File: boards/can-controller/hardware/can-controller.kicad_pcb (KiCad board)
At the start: 2 copper layers, 100 x 100 mm, 186 parts, among them J1 RPi_GPIO, J10 CAN1, J11 CAN2, J12 CAN3, J13 CAN4, J2 ICSP, J20 12V IN, J3 UART, J30 RELAY, J4 USB-C, J40 GPIO, J50 ANALOG, Q1 SUD50P04-08, U1 PIC32MK1024MCM064-I/PT, U10 ISO1044BD, U11 ISO1044BD, U12 ISO1044BD, U13 ISO1044BD, U2 MCP1826S-3302E/DB, U20 R-78E5.0-0.5, U21 TLP293, U3 USBLC6-2SC6, U30 ISO6740, U31 ISO6740, U32 ULN2803A, U33 MCP23008-E/SO, U50 MCP3428-E/SL, U60 MCP4922-E/SL, U61 LM4040-2.5, U62 LM358B, U63 TPS61040, Y1 12MHz

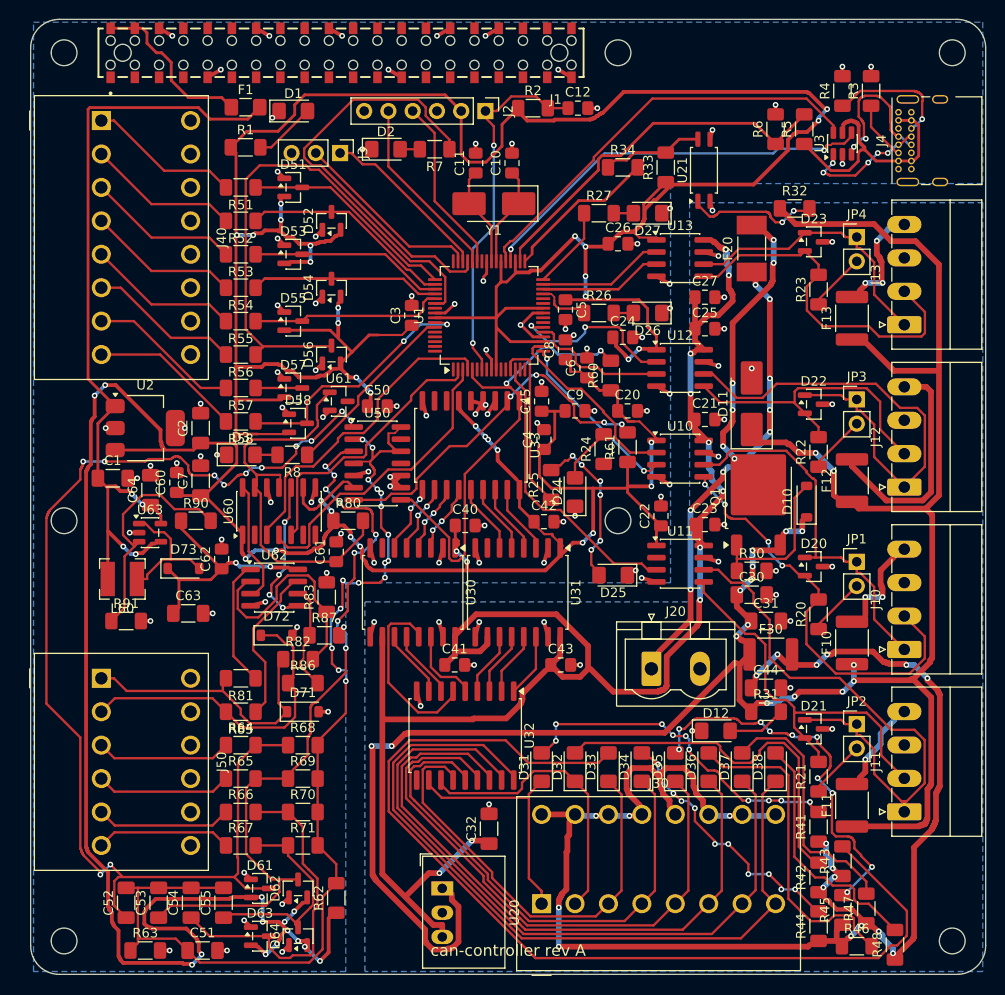
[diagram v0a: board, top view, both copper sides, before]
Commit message: can-controller: rev 6 snapshot (placement, domain pours, ground fanout); POC plan
- PCB reset to 100 x 100 mm with M4 standoff holes, synced from the new
  schematic, first-pass placement (place_rev6.py), domain pours and 2 mm
  isolation keep-outs (zones_rev6.py), 117 ground fanout vias (route_rev6.py).
  Not routed: 100 x 100 mm on 2 layers proved unroutable (Freerouting
  plateaued at ~40 unrouted).
- Net classes: Default 0.2 mm, Power 0.5 mm, PowerQFP 0.25 mm.
- Relay flyback diodes 1N4148W (SOD-123).
- tools/miniroute.py: island joining at cut ends, skips unreachable islands.
- Requirements 4.0: subsystem proof-of-concept boards (<= 100 x 100 mm) and a
  pluggable PIC + power module first; final board <= 115 x 170 mm.

Co-Authored-By: Claude Opus 5.5 <noreply@anthropic.com>
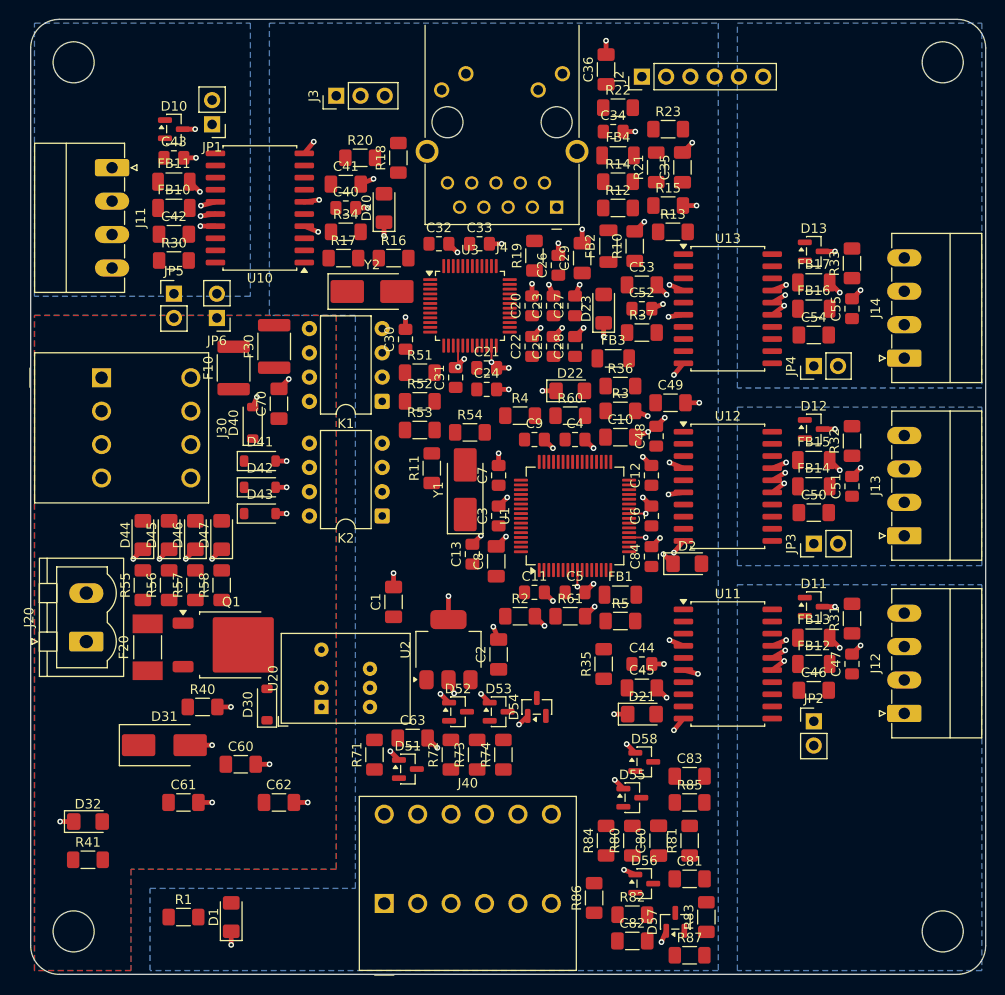
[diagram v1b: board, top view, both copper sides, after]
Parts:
- removed C64: 10uF 25V X7R, Capacitor_SMD:C_1206_3216Metric_Pad1.33x1.80mm_HandSolder
- removed D24, D25, D26, D27: LED yellow, LED_SMD:LED_1206_3216Metric_Pad1.42x1.75mm_HandSolder
- removed D3: LED green, LED_SMD:LED_1206_3216Metric_Pad1.42x1.75mm_HandSolder
- removed D33, D34, D35, D36, D37, D38: LED red, LED_SMD:LED_1206_3216Metric_Pad1.42x1.75mm_HandSolder
- removed D61, D62, D63, D64: BAT54S, Package_TO_SOT_SMD:SOT-23
- removed D71, D72: 15V, Diode_SMD:D_SOD-123
- removed D73: MBR0530, Diode_SMD:D_SOD-123
- removed F1: 0.75A, Fuse:Fuse_1206_3216Metric_Pad1.42x1.75mm_HandSolder
- removed F11, F12, F13: 1.1A, Fuse:Fuse_1812_4532Metric_Pad1.30x3.40mm_HandSolder
- removed J1: RPi_GPIO, Thl_Connector:Samtec_REF-182665_2x20_P2.54mm_PassThrough
- removed J10: CAN1, Connector_Phoenix_MC:PhoenixContact_MC_1,5_4-G-3.5_1x04_P3.50mm_Horizontal
- removed J50: ANALOG, Thl_Connector:PhoenixContact_SPTD_1,5_6-H-3,5_2x06_P3.5mm_Horizontal
- removed L60: 10uH, Inductor_SMD:L_Bourns-SRN4018
- removed MH5, MH6, MH7: MountingHole_2.7mm_M2.5, MountingHole:MountingHole_2.7mm_M2.5
- removed R24, R25, R26, R27, R7, R8: 1k, Resistor_SMD:R_1206_3216Metric_Pad1.30x1.75mm_HandSolder
- removed R42, R43, R44, R45, R46, R47, R48: 4.7k, Resistor_SMD:R_1206_3216Metric_Pad1.30x1.75mm_HandSolder
- removed R6: 100k, Resistor_SMD:R_1206_3216Metric_Pad1.30x1.75mm_HandSolder
- removed R62, R63: 10k, Resistor_SMD:R_1206_3216Metric_Pad1.30x1.75mm_HandSolder
- removed R64, R65, R66, R67: 10M, Resistor_SMD:R_1206_3216Metric_Pad1.30x1.75mm_HandSolder
- removed R68, R69, R70: 130k, Resistor_SMD:R_1206_3216Metric_Pad1.30x1.75mm_HandSolder
- removed R90: 1M, Resistor_SMD:R_1206_3216Metric_Pad1.30x1.75mm_HandSolder
- removed R91: 105k, Resistor_SMD:R_1206_3216Metric_Pad1.30x1.75mm_HandSolder
- removed U21: TLP293, Package_SO:SOIC-4_4.55x2.6mm_P1.27mm
- removed U30, U31: ISO6740, Package_SO:SOIC-16W_7.5x10.3mm_P1.27mm
- removed U32: ULN2803A, Package_SO:SOIC-18W_7.5x11.6mm_P1.27mm
- removed U33: MCP23008-E/SO, Package_SO:SOIC-18W_7.5x11.6mm_P1.27mm
- removed U50: MCP3428-E/SL, Package_SO:SOIC-14_3.9x8.7mm_P1.27mm
- removed U60: MCP4922-E/SL, Package_SO:SOIC-14_3.9x8.7mm_P1.27mm
- removed U61: LM4040-2.5, Package_TO_SOT_SMD:SOT-23
- removed U62: LM358B, Package_SO:SOIC-8_3.9x4.9mm_P1.27mm
- removed U63: TPS61040, Package_TO_SOT_SMD:SOT-23-5
- added C13: 100nF 50V X7R, Capacitor_SMD:C_0805_2012Metric_Pad1.18x1.45mm_HandSolder, F.Cu at (146.2, 156.0)
- added C28: 100nF 50V X7R, Capacitor_SMD:C_0805_2012Metric_Pad1.18x1.45mm_HandSolder, F.Cu at (157.0, 134.2)
- added C29: 3.3uF 25V X7R, Capacitor_SMD:C_1206_3216Metric_Pad1.33x1.80mm_HandSolder, F.Cu at (157.8, 125.0)
- added C33: 100nF 50V X7R, Capacitor_SMD:C_0805_2012Metric_Pad1.18x1.45mm_HandSolder, F.Cu at (147.0, 123.5)
- added C34: 100nF 50V X7R, Capacitor_SMD:C_0805_2012Metric_Pad1.18x1.45mm_HandSolder, F.Cu at (161.0, 111.8)
- added C35: 1uF 50V X7R, Capacitor_SMD:C_1206_3216Metric_Pad1.33x1.80mm_HandSolder, F.Cu at (168.2, 115.5)
- added C36: 1nF 2kV X7R, Capacitor_SMD:C_1206_3216Metric_Pad1.33x1.80mm_HandSolder, F.Cu at (160.2, 105.2)
- added C46: 10uF 25V X7R, Capacitor_SMD:C_1206_3216Metric_Pad1.33x1.80mm_HandSolder, F.Cu at (182.0, 170.2)
- added C47: 100nF 50V X7R, Capacitor_SMD:C_0805_2012Metric_Pad1.18x1.45mm_HandSolder, F.Cu at (186.0, 167.5)
- added C48: 100nF 50V X7R, Capacitor_SMD:C_0805_2012Metric_Pad1.18x1.45mm_HandSolder, F.Cu at (165.5, 143.7)
- added C49: 10uF 25V X7R, Capacitor_SMD:C_1206_3216Metric_Pad1.33x1.80mm_HandSolder, F.Cu at (167.0, 140.2)
- added C70: 10uF 25V X7R, Capacitor_SMD:C_1206_3216Metric_Pad1.33x1.80mm_HandSolder, F.Cu at (126.0, 140.2)
- added C80: 100nF 50V X7R, Capacitor_SMD:C_1206_3216Metric_Pad1.33x1.80mm_HandSolder, F.Cu at (165.8, 186.0)
- added C81: 100nF 50V X7R, Capacitor_SMD:C_1206_3216Metric_Pad1.33x1.80mm_HandSolder, F.Cu at (169.0, 190.0)
- added C82: 100nF 50V X7R, Capacitor_SMD:C_1206_3216Metric_Pad1.33x1.80mm_HandSolder, F.Cu at (163.0, 196.5)
- added C83: 100nF 50V X7R, Capacitor_SMD:C_1206_3216Metric_Pad1.33x1.80mm_HandSolder, F.Cu at (169.0, 179.2)
- added C84: 100nF 50V X7R, Capacitor_SMD:C_0805_2012Metric_Pad1.18x1.45mm_HandSolder, F.Cu at (165.0, 156.2)
- added D13: NUP2105L, Package_TO_SOT_SMD:SOT-23, F.Cu at (182.0, 124.3)
- added D30: 15V, Diode_SMD:D_SOD-123, F.Cu at (124.8, 171.8)
- added D40: 1N4148W, Diode_SMD:D_SOD-123, F.Cu at (123.2, 142.2)
- added D41: 1N4148W, Diode_SMD:D_SOD-123, F.Cu at (124.0, 146.2)
- added D42: 1N4148W, Diode_SMD:D_SOD-123, F.Cu at (124.0, 149.0)
- added D43: 1N4148W, Diode_SMD:D_SOD-123, F.Cu at (124.0, 151.8)
- added D44: LED red, LED_SMD:LED_1206_3216Metric_Pad1.42x1.75mm_HandSolder, F.Cu at (111.8, 154.0)
- added D45: LED red, LED_SMD:LED_1206_3216Metric_Pad1.42x1.75mm_HandSolder, F.Cu at (114.5, 154.0)
- added D46: LED red, LED_SMD:LED_1206_3216Metric_Pad1.42x1.75mm_HandSolder, F.Cu at (117.2, 154.0)
- added D47: LED red, LED_SMD:LED_1206_3216Metric_Pad1.42x1.75mm_HandSolder, F.Cu at (120.0, 154.0)
- added FB1: HI1206P121R-10, Inductor_SMD:L_1206_3216Metric_Pad1.22x1.90mm_HandSolder, F.Cu at (161.8, 160.2)
- added FB10: BLM31KN102SN1L, Inductor_SMD:L_1206_3216Metric_Pad1.22x1.90mm_HandSolder, F.Cu at (115.0, 119.8)
- added FB11: BLM31KN102SN1L, Inductor_SMD:L_1206_3216Metric_Pad1.22x1.90mm_HandSolder, F.Cu at (115.0, 117.0)
- added FB12: BLM31KN102SN1L, Inductor_SMD:L_1206_3216Metric_Pad1.22x1.90mm_HandSolder, F.Cu at (182.0, 167.5)
- added FB13: BLM31KN102SN1L, Inductor_SMD:L_1206_3216Metric_Pad1.22x1.90mm_HandSolder, F.Cu at (182.0, 164.8)
- added FB14: BLM31KN102SN1L, Inductor_SMD:L_1206_3216Metric_Pad1.22x1.90mm_HandSolder, F.Cu at (182.0, 148.9)
- added FB15: BLM31KN102SN1L, Inductor_SMD:L_1206_3216Metric_Pad1.22x1.90mm_HandSolder, F.Cu at (182.0, 146.2)
- added FB16: BLM31KN102SN1L, Inductor_SMD:L_1206_3216Metric_Pad1.22x1.90mm_HandSolder, F.Cu at (182.0, 130.3)
- added FB17: BLM31KN102SN1L, Inductor_SMD:L_1206_3216Metric_Pad1.22x1.90mm_HandSolder, F.Cu at (182.0, 127.5)
- added FB2: HI1206P121R-10, Inductor_SMD:L_1206_3216Metric_Pad1.22x1.90mm_HandSolder, F.Cu at (160.5, 123.8)
- added FB3: HI1206P121R-10, Inductor_SMD:L_1206_3216Metric_Pad1.22x1.90mm_HandSolder, F.Cu at (161.0, 135.5)
- added FB4: HI1206P121R-10, Inductor_SMD:L_1206_3216Metric_Pad1.22x1.90mm_HandSolder, F.Cu at (161.5, 114.2)
- added J14: CAN4, Connector_Phoenix_MC:PhoenixContact_MC_1,5_4-G-3.5_1x04_P3.50mm_Horizontal, F.Cu at (191.5, 135.5)
- added JP5: POWERED GND, Connector_PinHeader_2.54mm:PinHeader_1x02_P2.54mm_Vertical, F.Cu at (115.0, 128.7)
- added JP6: POWERED 12V, Connector_PinHeader_2.54mm:PinHeader_1x02_P2.54mm_Vertical, F.Cu at (119.5, 131.3)
- added K1: AQW212, Package_DIP:DIP-8_W7.62mm, F.Cu at (136.8, 140.0)
- added K2: AQW212, Package_DIP:DIP-8_W7.62mm, F.Cu at (136.8, 152.0)
- added R10: 10k, Resistor_SMD:R_1206_3216Metric_Pad1.30x1.75mm_HandSolder, F.Cu at (163.2, 123.8)
- added R11: 10k, Resistor_SMD:R_1206_3216Metric_Pad1.30x1.75mm_HandSolder, F.Cu at (142.0, 147.0)
- added R12: 10k, Resistor_SMD:R_1206_3216Metric_Pad1.30x1.75mm_HandSolder, F.Cu at (161.5, 119.8)
- added R13: 10k, Resistor_SMD:R_1206_3216Metric_Pad1.30x1.75mm_HandSolder, F.Cu at (167.2, 122.2)
- added R14: 12k, Resistor_SMD:R_1206_3216Metric_Pad1.30x1.75mm_HandSolder, F.Cu at (161.5, 117.0)
- added R15: 300R, Resistor_SMD:R_1206_3216Metric_Pad1.30x1.75mm_HandSolder, F.Cu at (166.8, 119.5)
- added R16: 1M, Resistor_SMD:R_1206_3216Metric_Pad1.30x1.75mm_HandSolder, F.Cu at (138.0, 125.0)
- added R17: 49.9R, Resistor_SMD:R_1206_3216Metric_Pad1.30x1.75mm_HandSolder, F.Cu at (132.8, 125.0)
- added R18: 49.9R, Resistor_SMD:R_1206_3216Metric_Pad1.30x1.75mm_HandSolder, F.Cu at (138.5, 114.5)
- added R19: 49.9R, Resistor_SMD:R_1206_3216Metric_Pad1.30x1.75mm_HandSolder, F.Cu at (152.8, 124.8)
- added R35: 1k, Resistor_SMD:R_1206_3216Metric_Pad1.30x1.75mm_HandSolder, F.Cu at (160.0, 167.5)
- added R36: 1k, Resistor_SMD:R_1206_3216Metric_Pad1.30x1.75mm_HandSolder, F.Cu at (161.8, 138.4)
- added R37: 1k, Resistor_SMD:R_1206_3216Metric_Pad1.30x1.75mm_HandSolder, F.Cu at (164.0, 132.8)
- added R40: 10k, Resistor_SMD:R_1206_3216Metric_Pad1.30x1.75mm_HandSolder, F.Cu at (118.0, 172.0)
- added R72: 330R, Resistor_SMD:R_1206_3216Metric_Pad1.30x1.75mm_HandSolder, F.Cu at (144.0, 177.0)
- added R73: 330R, Resistor_SMD:R_1206_3216Metric_Pad1.30x1.75mm_HandSolder, F.Cu at (146.8, 177.0)
- added R74: 330R, Resistor_SMD:R_1206_3216Metric_Pad1.30x1.75mm_HandSolder, F.Cu at (149.5, 177.0)
- added R84: 130k, Resistor_SMD:R_1206_3216Metric_Pad1.30x1.75mm_HandSolder, F.Cu at (160.2, 186.0)
- added Y2: 25MHz, Crystal:Crystal_SMD_5032-2Pin_5.0x3.2mm_HandSoldering, F.Cu at (135.8, 128.5)
- C10: value 27pF 50V C0G -> 1uF 50V X7R; footprint Capacitor_SMD:C_0805_2012Metric_Pad1.18x1.45mm_HandSolder -> Capacitor_SMD:C_1206_3216Metric_Pad1.33x1.80mm_HandSolder
- C12: value 100nF 50V X7R -> 27pF 50V C0G
- C30, C31: value 10uF 25V X7R -> 8pF 50V C0G; footprint Capacitor_SMD:C_1206_3216Metric_Pad1.33x1.80mm_HandSolder -> Capacitor_SMD:C_0805_2012Metric_Pad1.18x1.45mm_HandSolder
- C32, C44, C51, C7: value 10uF 25V X7R -> 100nF 50V X7R; footprint Capacitor_SMD:C_1206_3216Metric_Pad1.33x1.80mm_HandSolder -> Capacitor_SMD:C_0805_2012Metric_Pad1.18x1.45mm_HandSolder
- C41, C42, C45, C50, C60, C61, C62, C8: value 100nF 50V X7R -> 10uF 25V X7R; footprint Capacitor_SMD:C_0805_2012Metric_Pad1.18x1.45mm_HandSolder -> Capacitor_SMD:C_1206_3216Metric_Pad1.33x1.80mm_HandSolder
- C52, C55: footprint Capacitor_SMD:C_1206_3216Metric_Pad1.33x1.80mm_HandSolder -> Capacitor_SMD:C_0805_2012Metric_Pad1.18x1.45mm_HandSolder
- C53, C54: value 100nF 50V X7R -> 10uF 25V X7R
- C63: value 4.7uF 25V X7R -> 10uF 25V X7R
- D10: value 15V -> NUP2105L; footprint Diode_SMD:D_SOD-123 -> Package_TO_SOT_SMD:SOT-23
- D11: value SMBJ15A -> NUP2105L; footprint Diode_SMD:D_SMB_Handsoldering -> Package_TO_SOT_SMD:SOT-23
- D12: value LED green -> NUP2105L; footprint LED_SMD:LED_1206_3216Metric_Pad1.42x1.75mm_HandSolder -> Package_TO_SOT_SMD:SOT-23
- D20, D21, D22, D23: value NUP2105L -> LED yellow; footprint Package_TO_SOT_SMD:SOT-23 -> LED_SMD:LED_1206_3216Metric_Pad1.42x1.75mm_HandSolder
- D31: value LED red -> SMBJ15A; footprint LED_SMD:LED_1206_3216Metric_Pad1.42x1.75mm_HandSolder -> Diode_SMD:D_SMB_Handsoldering
- D32: value LED red -> LED green
- F10: value 1.1A -> 2A
- J11: value CAN2 -> CAN1
- J12: value CAN3 -> CAN2
- J13: value CAN4 -> CAN3
- J30: footprint Thl_Connector:PhoenixContact_SPTD_1,5_8-H-3,5_2x08_P3.5mm_Horizontal -> Thl_Connector:PhoenixContact_SPTD_1,5_4-H-3,5_2x04_P3.5mm_Horizontal
- J4: value USB-C -> JD0-0004NL; footprint Connector_USB:USB_C_Receptacle_GCT_USB4085 -> Thl_Connector:RJ45_Pulse_JD0-0004NL_Horizontal
- J40: value GPIO -> IO; footprint Thl_Connector:PhoenixContact_SPTD_1,5_8-H-3,5_2x08_P3.5mm_Horizontal -> Thl_Connector:PhoenixContact_SPTD_1,5_6-H-3,5_2x06_P3.5mm_Horizontal
- MH1, MH2, MH3, MH4: value MountingHole_2.7mm_M2.5 -> MountingHole_4.3mm_M4_Standoff7mm; footprint MountingHole:MountingHole_2.7mm_M2.5 -> Thl_Mechanical:MountingHole_4.3mm_M4_Standoff7mm
- R20: value 120R -> 49.9R
- R21: value 120R -> 0R
- R22, R23: value 120R -> 330R
- R3, R4: value 5.1k -> 10k
- R30, R32, R33: value 10k -> 120R
- R31: value 4.7k -> 120R
- R51, R52, R53, R54: value 4.7k -> 470R
- R60, R61: value 4.7k -> 10k
- R71: value 130k -> 330R
- R80: value 1k -> 10M
- R81: value 470R -> 10M
- R82: value 30k -> 10M
- R83: value 10k -> 10M
- R85: value 470R -> 130k
- R86: value 30k -> 130k
- R87: value 10k -> 130k
- U10, U11, U12, U13: value ISO1044BD -> ISOW1044; footprint Package_SO:SOIC-8_3.9x4.9mm_P1.27mm -> Package_SO:SOIC-20W_7.5x12.8mm_P1.27mm
- U20: value R-78E5.0-0.5 -> TDN 5-2411WI; footprint Converter_DCDC:Converter_DCDC_RECOM_R-78E-0.5_THT -> Converter_DCDC:Converter_DCDC_TRACO_TDN_5-xxxxWI_THT
- U3: value USBLC6-2SC6 -> W6100-L; footprint Package_TO_SOT_SMD:SOT-23-6 -> Package_QFP:LQFP-48_7x7mm_P0.5mm
- moved J11 106.9 mm to (108.5, 115.5), turned to -90 degrees
- moved C55 90.5 mm to (186.0, 130.3)
- moved C54 88.2 mm to (182.0, 133.1), turned to 0 degrees
- moved J40 87.2 mm to (137.0, 192.6), turned to 0 degrees
- moved D1 84.6 mm to (121.0, 194.0), turned to 90 degrees
- moved C51 83.6 mm to (186.0, 148.9), turned to 90 degrees
- moved C52 82.4 mm to (164.0, 130.3), turned to 0 degrees
- moved C53 82.1 mm to (164.0, 127.8), turned to 0 degrees
- moved JP1 81.6 mm to (119.0, 111.0), turned to 180 degrees
- moved R1 80.9 mm to (116.0, 194.0)
- moved D10 76.9 mm to (115.0, 111.5), turned to 0 degrees
- moved R41 76.6 mm to (106.0, 188.0), turned to 0 degrees
- moved F20 75.8 mm to (112.2, 165.8)
- moved J30 71.8 mm to (107.4, 137.5), turned to -90 degrees
- moved F10 70.9 mm to (121.2, 136.5)
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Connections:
- net /12 V input/V12_F renamed /12 V input, logic supply/V12_F
- net /12 V input/V12_IN renamed /12 V input, logic supply/V12_IN
- net /MCU, USB, power/D1_A renamed /MCU, logic power/D1_A
- net /MCU, USB, power/PGC2 renamed /MCU, logic power/PGC2
- net /MCU, USB, power/PGD2 renamed /MCU, logic power/PGD2
- C10 pad 1: /MCU, USB, power/OSC1 -> /MCU, logic power/AVDD
- C11 pad 1: /MCU, USB, power/OSC2 -> /MCU, logic power/OSC1
- C12 pad 1: /MCU, USB, power/MCLR -> /MCU, logic power/OSC2
- C20 pad 1: +3V3 -> /Ethernet/1V2D
- C21 pad 1: V5_BUS -> /Ethernet/1V2D
- C21 pad 2: GND_BUS -> GND
- C22 pad 1: +3V3 -> /Ethernet/1V2D
- C23 pad 1: V5_BUS -> /Ethernet/1V2D
- C23 pad 2: GND_BUS -> GND
- C24 pad 1: +3V3 -> /Ethernet/1V2A
- C25 pad 1: V5_BUS -> +3V3
- C25 pad 2: GND_BUS -> GND
- C27 pad 1: V5_BUS -> /Ethernet/3V3A
- C27 pad 2: GND_BUS -> GND
- C30 pad 1: +12V -> /Ethernet/XSCI
- C30 pad 2: GND_BUS -> GND
- C31 pad 1: +12V -> /Ethernet/XSCO
- C31 pad 2: GND_BUS -> GND
- C32 pad 1: V5_BUS -> /Ethernet/TXCT
- C32 pad 2: GND_BUS -> GND
- C41 pad 1: V5_BUS -> +5V
- C41 pad 2: GND_BUS -> GND
- C42 pad 1: +3V3 -> /CAN x4/VISO1
- C42 pad 2: GND -> /CAN x4/GND2_1
- C43 pad 1: V5_BUS -> /CAN x4/VCAN1
- C43 pad 2: GND_BUS -> /CAN x4/GND_CAN1
- C44 pad 1: /Relay drive/V12_RLY -> +3V3
- C44 pad 2: GND_BUS -> GND
- C45 pad 1: +3V3 -> +5V
- C50 pad 1: +3V3 -> /CAN x4/VISO3
- C50 pad 2: GND -> /CAN x4/GND2_3
- C51 pad 1: /Analog in/VMID -> /CAN x4/VCAN3
- C51 pad 2: GND -> /CAN x4/GND_CAN3
- C52 pad 1: /Analog in/AIN1 -> +3V3
- C52 pad 2: /Analog in/VMID -> GND
- C53 pad 1: /Analog in/AIN2 -> +5V
- C53 pad 2: /Analog in/VMID -> GND
- C54 pad 1: /Analog in/AIN3 -> /CAN x4/VISO4
- C54 pad 2: /Analog in/VMID -> /CAN x4/GND2_4
- C55 pad 1: /Analog in/AIN4 -> /CAN x4/VCAN4
- C55 pad 2: /Analog in/VMID -> /CAN x4/GND_CAN4
- C60 pad 1: +3V3 -> +12V
- C60 pad 2: GND -> GND_RACK
- C61 pad 1: /Analog out/VREF -> +12V
- C61 pad 2: GND -> GND_RACK
- C62 pad 1: /Analog out/V13 -> +12V
- C62 pad 2: GND -> GND_RACK
- C63 pad 1: /Analog out/V13 -> +5V
- C9 pad 1: +3V3 -> /MCU, logic power/AVDD
- D10 pad 1: +12V -> /CAN x4/CANH1
- D10 pad 2: /12 V input/Q1_G -> /CAN x4/CANL1
- D11 pad 1: +12V -> /CAN x4/CANH2
- D11 pad 2: GND_BUS -> /CAN x4/CANL2
- D12 pad 1: GND_BUS -> /CAN x4/CANH3
- D12 pad 2: /12 V input/D12_A -> /CAN x4/CANL3
- D2 pad 2: /MCU, USB, power/D2_A -> /MCU, logic power/D2_A
- D20 pad 1: /CAN x4/CANH1 -> GND
- D20 pad 2: /CAN x4/CANL1 -> /CAN x4/D20_A
- D21 pad 1: /CAN x4/CANH2 -> GND
- D21 pad 2: /CAN x4/CANL2 -> /CAN x4/D21_A
- D22 pad 1: /CAN x4/CANH3 -> GND
- D22 pad 2: /CAN x4/CANL3 -> /CAN x4/D22_A
- D23 pad 1: /CAN x4/CANH4 -> GND
- D23 pad 2: /CAN x4/CANL4 -> /CAN x4/D23_A
- D31 pad 1: /Relay drive/RLYO1 -> +12V
- D31 pad 2: /Relay drive/D31_A -> GND_RACK
- D32 pad 1: /Relay drive/RLYO2 -> GND_RACK
- D32 pad 2: /Relay drive/D32_A -> /12 V input, logic supply/D32_A
- D55 pad 3: GPIO5 -> AI1P
- D56 pad 3: GPIO6 -> AI1N
- D57 pad 3: GPIO7 -> AI2P
- D58 pad 3: GPIO8 -> AI2N
- F10 pad 2: /CAN x4/V12_CAN1 -> /CAN x4/V12_F10
- J11 pad 1: /CAN x4/CANH2 -> /CAN x4/CANH1
- J11 pad 2: /CAN x4/CANL2 -> /CAN x4/CANL1
- J11 pad 3: GND_BUS -> /CAN x4/GND_CAN1
- J11 pad 4: /CAN x4/V12_CAN2 -> /CAN x4/V12_CAN1
- J12 pad 1: /CAN x4/CANH3 -> /CAN x4/CANH2
- J12 pad 2: /CAN x4/CANL3 -> /CAN x4/CANL2
- J12 pad 3: GND_BUS -> /CAN x4/GND_CAN2
- J12 pad 4: /CAN x4/V12_CAN3 -> unconnected-(J12-Pin_4-Pad4)
- J13 pad 1: /CAN x4/CANH4 -> /CAN x4/CANH3
- J13 pad 2: /CAN x4/CANL4 -> /CAN x4/CANL3
- J13 pad 3: GND_BUS -> /CAN x4/GND_CAN3
- J13 pad 4: /CAN x4/V12_CAN4 -> unconnected-(J13-Pin_4-Pad4)
- J2 pad 1: /MCU, USB, power/MCLR -> /MCU, logic power/MCLR
- J20 pad 2: GND_BUS -> GND_RACK
- J3 pad 1: /MCU, USB, power/U1TX -> /MCU, logic power/U1TX
- J3 pad 2: /MCU, USB, power/U1RX -> /MCU, logic power/U1RX
- J30 pad 1: /Relay drive/RLYO1 -> /Relay drive/RLYOUT1
- J30 pad 2: /Relay drive/RLYO2 -> /Relay drive/RLYOUT2
- J30 pad 3: /Relay drive/RLYO3 -> /Relay drive/RLYOUT3
- J30 pad 4: /Relay drive/RLYO4 -> /Relay drive/RLYOUT4
- J30 pad 5: /Relay drive/RLYO5 -> GND_RACK
- J30 pad 6: /Relay drive/RLYO6 -> GND_RACK
- J30 pad 7: /Relay drive/RLYO7 -> GND_RACK
- J30 pad 8: /Relay drive/RLYO8 -> GND_RACK
- J4 pad SH: GND -> /Ethernet/CHASSIS
- J40 pad 1: /GPIO/GPIO1_EXT -> /GPIO, analog in/GPIO1_EXT
- J40 pad 11: GND -> /GPIO, analog in/AI1N_EXT
- J40 pad 12: GND -> /GPIO, analog in/AI2N_EXT
- J40 pad 2: /GPIO/GPIO2_EXT -> /GPIO, analog in/GPIO2_EXT
- J40 pad 3: /GPIO/GPIO3_EXT -> /GPIO, analog in/GPIO3_EXT
- J40 pad 4: /GPIO/GPIO4_EXT -> /GPIO, analog in/GPIO4_EXT
- J40 pad 5: /GPIO/GPIO5_EXT -> /GPIO, analog in/AI1P_EXT
- J40 pad 6: /GPIO/GPIO6_EXT -> /GPIO, analog in/AI2P_EXT
- J40 pad 7: /GPIO/GPIO7_EXT -> GND
- J40 pad 8: /GPIO/GPIO8_EXT -> GND
- Q1 pad 1: /12 V input/Q1_G -> /12 V input, logic supply/Q1_G
- R2 pad 1: +3V3 -> /MCU, logic power/USB_DP
- R2 pad 2: /MCU, USB, power/MCLR -> GND
- R20 pad 1: /CAN x4/TERM1 -> /Ethernet/RXCT
- R20 pad 2: /CAN x4/CANL1 -> /Ethernet/RXN
- R21 pad 1: /CAN x4/TERM2 -> /Ethernet/3V3A
- R21 pad 2: /CAN x4/CANL2 -> /Ethernet/JCT
- R22 pad 1: /CAN x4/TERM3 -> +3V3
- R22 pad 2: /CAN x4/CANL3 -> /Ethernet/LEDG_A
- R23 pad 1: /CAN x4/TERM4 -> +3V3
- R23 pad 2: /CAN x4/CANL4 -> /Ethernet/LEDY_A
- R3 pad 1: /MCU, USB, power/CC1 -> /MCU, logic power/USB_DN
- R30 pad 1: /12 V input/Q1_G -> /CAN x4/TERM1
- R30 pad 2: GND_BUS -> /CAN x4/CANL1
- R31 pad 1: +12V -> /CAN x4/TERM2
- R31 pad 2: /12 V input/D12_A -> /CAN x4/CANL2
- R32 pad 1: +12V -> /CAN x4/TERM3
- R32 pad 2: /12 V input/OPTO_A -> /CAN x4/CANL3
- R33 pad 1: +3V3 -> /CAN x4/TERM4
- R33 pad 2: /12 V input/V12_OK_C -> /CAN x4/CANL4
- R34 pad 1: /12 V input/V12_OK_C -> LED_CAN1
- R34 pad 2: V12_OK -> /CAN x4/D20_A
- R4 pad 1: /MCU, USB, power/CC2 -> +3V3
- R4 pad 2: GND -> /MCU, logic power/MCLR
- R41 pad 1: /Relay drive/V12_RLY -> +12V
- R41 pad 2: /Relay drive/D31_A -> /12 V input, logic supply/D32_A
- R5 pad 1: /MCU, USB, power/VBUS_C -> /MCU, logic power/LED_HB
- R5 pad 2: /MCU, USB, power/VBUS -> /MCU, logic power/D2_A
- R51 pad 1: GPIO1 -> RLY1
- R51 pad 2: /GPIO/GPIO1_EXT -> /Relay drive/RLED1
- R52 pad 1: GPIO2 -> RLY2
- R52 pad 2: /GPIO/GPIO2_EXT -> /Relay drive/RLED2
- R53 pad 1: GPIO3 -> RLY3
- R53 pad 2: /GPIO/GPIO3_EXT -> /Relay drive/RLED3
- R54 pad 1: GPIO4 -> RLY4
- R54 pad 2: /GPIO/GPIO4_EXT -> /Relay drive/RLED4
- R55 pad 1: GPIO5 -> /Relay drive/RLYOUT1
- R55 pad 2: /GPIO/GPIO5_EXT -> /Relay drive/D44_A
- R56 pad 1: GPIO6 -> /Relay drive/RLYOUT2
- R56 pad 2: /GPIO/GPIO6_EXT -> /Relay drive/D45_A
- R57 pad 1: GPIO7 -> /Relay drive/RLYOUT3
- R57 pad 2: /GPIO/GPIO7_EXT -> /Relay drive/D46_A
- R58 pad 1: GPIO8 -> /Relay drive/RLYOUT4
- R58 pad 2: /GPIO/GPIO8_EXT -> /Relay drive/D47_A
- R60 pad 2: I2C_SCL -> VMID_REF
- R61 pad 1: +3V3 -> VMID_REF
- R61 pad 2: I2C_SDA -> GND
- R71 pad 1: /Analog in/AIN4 -> GPIO1
- R71 pad 2: /Analog in/VMID -> /GPIO, analog in/GPIO1_EXT
- R80 pad 1: +3V3 -> /GPIO, analog in/AI1P_EXT
- R80 pad 2: /Analog out/VREF -> AI1P
- R81 pad 1: /Analog out/OA1 -> /GPIO, analog in/AI1N_EXT
- R81 pad 2: /Analog out/AO1_EXT -> AI1N
- R82 pad 1: /Analog out/AO1_EXT -> /GPIO, analog in/AI2P_EXT
- R82 pad 2: /Analog out/FB1 -> AI2P
- R83 pad 1: /Analog out/FB1 -> /GPIO, analog in/AI2N_EXT
- R83 pad 2: GND -> AI2N
- R85 pad 1: /Analog out/OA2 -> AI1N
- R85 pad 2: /Analog out/AO2_EXT -> VMID
- R86 pad 1: /Analog out/AO2_EXT -> AI2P
- R86 pad 2: /Analog out/FB2 -> VMID
- R87 pad 1: /Analog out/FB2 -> AI2N
- R87 pad 2: GND -> VMID
- U1 pad 11: unconnected-(U1-RA12/AN10/RPA12-Pad11) -> LED_CAN3
- U1 pad 12: unconnected-(U1-RA11/AN9/RPA11-Pad12) -> LED_CAN4
- U1 pad 13: LED_CAN2 -> unconnected-(U1-RA0/OA2OUT/AN0/C2IN4-/C4IN3-/RPA0-Pad13)
- U1 pad 16: LED_CAN1 -> unconnected-(U1-RB1/PGC3/OA1OUT/VREF+/AN3/C1IN4-/C4IN2-/RPB1/CTED1-Pad16)
- U1 pad 19: +3V3 -> /MCU, logic power/AVDD
- U1 pad 2: DAC_SDI -> RLY1
- U1 pad 23: unconnected-(U1-RC2/OA3IN+/AN8/C3IN1+/C3IN3-/RPC2-Pad23) -> AI2N
- U1 pad 24: unconnected-(U1-RC11/AN11/C1IN2--Pad24) -> AI2P
- U1 pad 27: unconnected-(U1-RE12/AN12/C2IN2-/C5IN2-/SDA4-Pad27) -> AI1P
- U1 pad 28: unconnected-(U1-RE13/AN13/C3IN2-/SCL4-Pad28) -> AI1N
- U1 pad 29: LED_CAN3 -> unconnected-(U1-RE14/AN14/RPE14-Pad29)
- U1 pad 3: DAC_SCK -> RLY2
- U1 pad 32: LED_CAN4 -> unconnected-(U1-RB4/RPB4/SCL2-Pad32)
- U1 pad 33: V12_OK -> VMID_REF
- U1 pad 34: /MCU, USB, power/VBUS -> GND
- U1 pad 36: /MCU, USB, power/USB_DN -> /MCU, logic power/USB_DN
- U1 pad 37: /MCU, USB, power/USB_DP -> /MCU, logic power/USB_DP
- U1 pad 39: /MCU, USB, power/OSC1 -> /MCU, logic power/OSC1
- U1 pad 4: DAC_CS -> RLY3
- U1 pad 40: /MCU, USB, power/OSC2 -> /MCU, logic power/OSC2
- U1 pad 42: unconnected-(U1-RD8-Pad42) -> /MCU, logic power/LED_HB
- U1 pad 45: /MCU, USB, power/LED_HB -> unconnected-(U1-RC10/DAC2/AN48/RPC10-Pad45)
- U1 pad 46: /MCU, USB, power/U1TX -> VMID
- U1 pad 47: /MCU, USB, power/U1RX -> unconnected-(U1-RC13/SOSCI/RPC13(in_only)-Pad47)
- U1 pad 49: GPIO1 -> VMID
- U1 pad 5: I2C_SCL -> RLY4
- U1 pad 50: GPIO2 -> /MCU, logic power/U1RX
- U1 pad 51: GPIO3 -> ETH_MISO
- U1 pad 52: GPIO4 -> ETH_MOSI
- U1 pad 53: GPIO5 -> ETH_CS
- U1 pad 54: GPIO6 -> ETH_INT
- U1 pad 55: GPIO7 -> ETH_SCK
- U1 pad 58: GPIO8 -> ETH_RST
- U1 pad 59: /MCU, USB, power/LED_USB -> /MCU, logic power/U1TX
- U1 pad 6: I2C_SDA -> LED_CAN1
- U1 pad 60: unconnected-(U1-RB10/RPB10-Pad60) -> GPIO1
- U1 pad 61: unconnected-(U1-RB11/RPB11-Pad61) -> GPIO2
- U1 pad 62: unconnected-(U1-RB12/RPB12-Pad62) -> GPIO3
- U1 pad 63: unconnected-(U1-RB13/RPB13/CTPLS-Pad63) -> GPIO4
- U1 pad 7: /MCU, USB, power/MCLR -> /MCU, logic power/MCLR
- U1 pad 8: unconnected-(U1-RG9/AN16/RPG9-Pad8) -> LED_CAN2
- U10 pad 2: C1TX -> unconnected-(U10-IN-Pad2)
- U10 pad 3: C1RX -> C1TX
- U10 pad 5: /CAN x4/CANL1 -> C1RX
- U10 pad 6: /CAN x4/CANH1 -> GND
- U10 pad 7: GND_BUS -> unconnected-(U10-NC-Pad7)
- U10 pad 8: V5_BUS -> unconnected-(U10-EN/FLT-Pad8)
- U11 pad 2: C2TX -> unconnected-(U11-IN-Pad2)
- U11 pad 3: C2RX -> C2TX
- U11 pad 5: /CAN x4/CANL2 -> C2RX
- U11 pad 6: /CAN x4/CANH2 -> GND
- U11 pad 7: GND_BUS -> unconnected-(U11-NC-Pad7)
- U11 pad 8: V5_BUS -> unconnected-(U11-EN/FLT-Pad8)
- U12 pad 2: C3TX -> unconnected-(U12-IN-Pad2)
- U12 pad 3: C3RX -> C3TX
- U12 pad 5: /CAN x4/CANL3 -> C3RX
- U12 pad 6: /CAN x4/CANH3 -> GND
- U12 pad 7: GND_BUS -> unconnected-(U12-NC-Pad7)
- U12 pad 8: V5_BUS -> unconnected-(U12-EN/FLT-Pad8)
- U13 pad 2: C4TX -> unconnected-(U13-IN-Pad2)
- U13 pad 3: C4RX -> C4TX
- U13 pad 5: /CAN x4/CANL4 -> C4RX
- U13 pad 6: /CAN x4/CANH4 -> GND
- U13 pad 7: GND_BUS -> unconnected-(U13-NC-Pad7)
- U13 pad 8: V5_BUS -> unconnected-(U13-EN/FLT-Pad8)
- U20 pad 2: GND_BUS -> GND_RACK
- U3 pad 1: /MCU, USB, power/USB_DP_C -> GND
- U3 pad 2: GND -> /Ethernet/TXN
- U3 pad 3: /MCU, USB, power/USB_DN_C -> /Ethernet/TXP
- U3 pad 4: /MCU, USB, power/USB_DN -> /Ethernet/1V2A
- U3 pad 5: /MCU, USB, power/VBUS_C -> /Ethernet/RXN
- U3 pad 6: /MCU, USB, power/USB_DP -> /Ethernet/RXP
- Y1 pad 1: /MCU, USB, power/OSC1 -> /MCU, logic power/OSC1
- Y1 pad 2: /MCU, USB, power/OSC2 -> /MCU, logic power/OSC2
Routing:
- net +3V3: track 577.7 -> 0.00 mm, vias 48 -> 0
- net +12V: track 230.7 -> 0.00 mm, vias 17 -> 0
- net V5_BUS: track 170.3 -> 0.00 mm, vias 10 -> 0
- net /Relay drive/V12_RLY: track 142.1 -> 0.00 mm, vias 19 -> 0
- net /Analog in/AIN1: track 124.1 -> 0.00 mm, vias 12 -> 0
- net /Analog in/VMID: track 110.2 -> 0.00 mm, vias 16 -> 0
- net /Relay drive/D33_A: track 104.3 -> 0.00 mm
- net +5V: track 83.7 -> 0.00 mm, vias 4 -> 0
- net /Relay drive/RLYO8: track 81.2 -> 0.00 mm
- net /Analog in/AIN2: track 77.6 -> 0.00 mm, vias 8 -> 0
- net /Relay drive/RLYO7: track 74.6 -> 0.00 mm
- net /Relay drive/RLYO6: track 67.9 -> 0.00 mm
- net /Relay drive/RLYO5: track 61.3 -> 0.00 mm
- net /CAN x4/CANH2: track 58.2 -> 0.00 mm
- net GPIO6: track 56.8 -> 0.00 mm
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- added copper zone on F.Cu, net +12V
- added copper zone on B.Cu, net /CAN x4/GND_CAN1
- added copper zone on B.Cu, net /CAN x4/GND_CAN2
- added copper zone on B.Cu, net /CAN x4/GND_CAN3
- added copper zone on B.Cu, net /CAN x4/GND_CAN4
- added copper zone on B.Cu, net GND_RACK
- removed copper zone on B.Cu, net GND_BUS
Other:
- board text removed: "12 V DOMAIN (GND_BUS)"
- board text removed: "Domain boundary (placement rev 2): only U10-U13, U21, U30, U31 cross it"
- board text removed: "LOGIC DOMAIN (GND)"
- board text removed: "can-controller rev ${REVISION}"

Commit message: Move core, can-card, io-card, serial-card, can-ssr, probe-helper to rev B
Rev A went to PCBWay and is tagged revA. Rev B replaces parts the Mouser
BOM check flagged (obsolete, end of life, not recommended for new designs,
or not orderable) and swaps out-of-stock passives and diodes for in-stock
equivalents. Field-only changes, same footprints, no layout change; the
reference boards (can-controller, pic-module) get the same part numbers.
The rev A order lists (DigiKey, Mouser) carry the same substitutions; the
Mouser list leaves out the T821 box headers (bought from DigiKey).

docs/rev-b-changes.md lists every change and the rev B to-dos (MAX7219 is
obsolete and must be replaced). transfer/mouser-revA.xlsx (Mouser BOM
check) consumed.

Co-Authored-By: Claude Opus 5.5 <noreply@anthropic.com>
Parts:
- FB10, FB11, FB12, FB13, FB14, FB15, FB16, FB17: value BLM31KN102SN1L -> BLM31KN102SH1L

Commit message: Rev B / rev A order: 10 uF CL31B106KAHZW6E, beads BLM31PG391SN1L
Both earlier substitutes (CL31B106KAHNNNE, BLM31KN102SH1L) are on
backorder at Mouser. CL31B106KAHZW6E has the same rating (1.4 mm tall).
The isolated-supply beads need no 1 kOhm: TI's reference uses 330 Ohm;
BLM31PG391SN1L is 390 Ohm @ 100 MHz, 2 A, 50 mOhm. Field-only changes;
order lists regenerated.

Co-Authored-By: Claude Opus 5.5 <noreply@anthropic.com>
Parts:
- FB10, FB11, FB12, FB13, FB14, FB15, FB16, FB17: value BLM31KN102SH1L -> BLM31PG391SN1L
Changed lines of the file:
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@@
 			)
 		)
-		(property "Value" "BLM31KN102SH1L"
+		(property "Value" "BLM31PG391SN1L"
 			(at 0 1.9 0)
 			(layer "F.Fab")
@@
 			)
 		)
-		(property "MPN" "BLM31KN102SH1L"
+		(property "MPN" "BLM31PG391SN1L"
 			(at 0 0 0)
 			(layer "F.Fab")
@@
 			)
 		)
-		(property "MPN" "CL31B106KAHNNNE"
+		(property "MPN" "CL31B106KAHZW6E"
 			(at 0 0 0)
 			(layer "F.Fab")
@@
 			)
 		)
-		(property "Value" "BLM31KN102SH1L"
+		(property "Value" "BLM31PG391SN1L"
 			(at 0 1.9 0)
 			(layer "F.Fab")
@@
 			)
 		)
-		(property "MPN" "BLM31KN102SH1L"
+		(property "MPN" "BLM31PG391SN1L"
 			(at 0 0 0)
 			(layer "F.Fab")
@@
 			)
 		)
-		(property "MPN" "CL31B106KAHNNNE"
+		(property "MPN" "CL31B106KAHZW6E"
 			(at 0 0 0)
 			(layer "F.Fab")
@@
 			)
 		)
-		(property "MPN" "CL31B106KAHNNNE"
+		(property "MPN" "CL31B106KAHZW6E"
 			(at 0 0 0)
 			(layer "F.Fab")
@@
 			)
 		)
-		(property "Value" "BLM31KN102SH1L"
+		(property "Value" "BLM31PG391SN1L"
 			(at 0 1.9 0)
 			(layer "F.Fab")
@@
 			)
 		)
-		(property "MPN" "BLM31KN102SH1L"
+		(property "MPN" "BLM31PG391SN1L"
 			(at 0 0 0)
 			(layer "F.Fab")
@@
 			)
 		)
-		(property "Value" "BLM31KN102SH1L"
+		(property "Value" "BLM31PG391SN1L"
 			(at 0 1.9 0)
 			(layer "F.Fab")
@@
 			)
 		)
-		(property "MPN" "BLM31KN102SH1L"
+		(property "MPN" "BLM31PG391SN1L"
 			(at 0 0 0)
 			(layer "F.Fab")
@@
 			)
 		)
-		(property "Value" "BLM31KN102SH1L"
+		(property "Value" "BLM31PG391SN1L"
 			(at 0 1.9 0)
 			(layer "F.Fab")
@@
 			)
 		)
-		(property "MPN" "BLM31KN102SH1L"
+		(property "MPN" "BLM31PG391SN1L"
 			(at 0 0 0)
 			(layer "F.Fab")
@@
 			)
 		)
-		(property "MPN" "CL31B106KAHNNNE"
+		(property "MPN" "CL31B106KAHZW6E"
 			(at 0 0 0)
 			(layer "F.Fab")
@@
 			)
 		)
-		(property "MPN" "CL31B106KAHNNNE"
+		(property "MPN" "CL31B106KAHZW6E"
 			(at 0 0 90)
 			(layer "F.Fab")
@@
 			)
 		)
-		(property "MPN" "CL31B106KAHNNNE"
+		(property "MPN" "CL31B106KAHZW6E"
 			(at 0 0 0)
 			(layer "F.Fab")
@@
 			)
 		)
-		(property "MPN" "CL31B106KAHNNNE"
+		(property "MPN" "CL31B106KAHZW6E"
 			(at 0 0 0)
 			(layer "F.Fab")
@@
 			)
 		)
-		(property "Value" "BLM31KN102SH1L"
+		(property "Value" "BLM31PG391SN1L"
 			(at 0 1.9 0)
 			(layer "F.Fab")
@@
 			)
 		)
-		(property "MPN" "BLM31KN102SH1L"
+		(property "MPN" "BLM31PG391SN1L"
 			(at 0 0 0)
 			(layer "F.Fab")
@@
 			)
 		)
-		(property "MPN" "CL31B106KAHNNNE"
+		(property "MPN" "CL31B106KAHZW6E"
 			(at 0 0 0)
 			(layer "F.Fab")
@@
 			)
 		)
-		(property "Value" "BLM31KN102SH1L"
+		(property "Value" "BLM31PG391SN1L"
 			(at 0 1.9 0)
 			(layer "F.Fab")
@@
 			)
 		)
-		(property "MPN" "BLM31KN102SH1L"
+		(property "MPN" "BLM31PG391SN1L"
 			(at 0 0 0)
 			(layer "F.Fab")
@@
 			)
 		)
-		(property "MPN" "CL31B106KAHNNNE"
+		(property "MPN" "CL31B106KAHZW6E"
 			(at 0 0 90)
 			(layer "F.Fab")
@@
 			)
 		)
-		(property "MPN" "CL31B106KAHNNNE"
+		(property "MPN" "CL31B106KAHZW6E"
 			(at 0 0 0)
 			(layer "F.Fab")
@@
 			)
 		)
-		(property "MPN" "CL31B106KAHNNNE"
+		(property "MPN" "CL31B106KAHZW6E"
 			(at 0 0 0)
 			(layer "F.Fab")
@@
 			)
 		)
-		(property "MPN" "CL31B106KAHNNNE"
+		(property "MPN" "CL31B106KAHZW6E"
 			(at 0 0 90)
 			(layer "F.Fab")
@@
 			)
 		)
-		(property "MPN" "CL31B106KAHNNNE"
+		(property "MPN" "CL31B106KAHZW6E"
 			(at 0 0 90)
 			(layer "F.Fab")
@@
 			)
 		)
-		(property "MPN" "CL31B106KAHNNNE"
+		(property "MPN" "CL31B106KAHZW6E"
 			(at 0 0 0)
 			(layer "F.Fab")
@@
 			)
 		)
-		(property "MPN" "CL31B106KAHNNNE"
+		(property "MPN" "CL31B106KAHZW6E"
 			(at 0 0 0)
 			(layer "F.Fab")
@@
 			)
 		)
-		(property "MPN" "CL31B106KAHNNNE"
+		(property "MPN" "CL31B106KAHZW6E"
 			(at 0 0 0)
 			(layer "F.Fab")
@@
 			)
 		)
-		(property "Value" "BLM31KN102SH1L"
+		(property "Value" "BLM31PG391SN1L"
 			(at 0 1.9 0)
 			(layer "F.Fab")
@@
 			)
 		)
-		(property "MPN" "BLM31KN102SH1L"
+		(property "MPN" "BLM31PG391SN1L"
 			(at 0 0 0)
 			(layer "F.Fab")

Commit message: Rev B / rev A order: ISOW1044BDFMR (ISOW1044DFMR out of stock)
Same TI part, package and pinout with basic instead of reinforced
isolation; the CAN buses are low-voltage and isolated against ground
loops, not for safety. Field-only change on can-card (and the reference
can-controller); order lists regenerated.

Co-Authored-By: Claude Opus 5.5 <noreply@anthropic.com>
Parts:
- U10, U11, U12, U13: value ISOW1044 -> ISOW1044B
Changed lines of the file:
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@@
 			)
 		)
-		(property "Value" "ISOW1044"
+		(property "Value" "ISOW1044B"
 			(at 0 7.35 0)
 			(layer "F.Fab")
@@
 			)
 		)
-		(property "MPN" "ISOW1044DFMR"
+		(property "MPN" "ISOW1044BDFMR"
 			(at 0 0 0)
 			(layer "F.Fab")
@@
 			)
 		)
-		(property "Value" "ISOW1044"
+		(property "Value" "ISOW1044B"
 			(at 0 7.35 0)
 			(layer "F.Fab")
@@
 			)
 		)
-		(property "MPN" "ISOW1044DFMR"
+		(property "MPN" "ISOW1044BDFMR"
 			(at 0 0 0)
 			(layer "F.Fab")
@@
 			)
 		)
-		(property "Value" "ISOW1044"
+		(property "Value" "ISOW1044B"
 			(at 0 7.35 0)
 			(layer "F.Fab")
@@
 			)
 		)
-		(property "MPN" "ISOW1044DFMR"
+		(property "MPN" "ISOW1044BDFMR"
 			(at 0 0 0)
 			(layer "F.Fab")
@@
 			)
 		)
-		(property "Value" "ISOW1044"
+		(property "Value" "ISOW1044B"
 			(at 0 7.35 180)
 			(layer "F.Fab")
@@
 			)
 		)
-		(property "MPN" "ISOW1044DFMR"
+		(property "MPN" "ISOW1044BDFMR"
 			(at 0 0 180)
 			(layer "F.Fab")

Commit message: Mouser cart: SQD50P04-09L P-FET, Diotec P6SMBJ15A TVS
Out of stock: Vishay SUD50P04-08-GE3 (core Q1) -> SQD50P04-09L_GE3 and
Littelfuse SMBJ15A (12 V input TVS) -> Diotec P6SMBJ15A, same footprints,
in core, can-ssr and the can-controller/pic-module references. Logged in
docs/rev-b-changes.md; order lists regenerated. The cart as ordered is
docs/orders/mouser-cart-2026-10-12.xls.

Co-Authored-By: Claude Opus 5.5 <noreply@anthropic.com>
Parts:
- D31: value SMBJ15A -> P6SMBJ15A
- Q1: value SUD50P04-08 -> SQD50P04-09L
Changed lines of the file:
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@@
 			)
 		)
-		(property "Value" "SMBJ15A"
+		(property "Value" "P6SMBJ15A"
 			(at 0 3 0)
 			(layer "F.Fab")
@@
 			)
 		)
-		(property "Manufacturer" "Littelfuse"
+		(property "Manufacturer" "Diotec Semiconductor"
 			(at 0 0 0)
 			(layer "F.Fab")
@@
 			)
 		)
-		(property "MPN" "SMBJ15A"
+		(property "MPN" "P6SMBJ15A"
 			(at 0 0 0)
 			(layer "F.Fab")
@@
 			)
 		)
-		(property "Value" "SUD50P04-08"
+		(property "Value" "SQD50P04-09L"
 			(at 0 4.5 0)
 			(layer "F.Fab")
@@
 			)
 		)
-		(property "MPN" "SUD50P04-08-GE3"
+		(property "MPN" "SQD50P04-09L_GE3"
 			(at 0 0 0)
 			(layer "F.Fab")
